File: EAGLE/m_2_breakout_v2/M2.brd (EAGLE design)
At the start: 73.3 x 101.6 mm, 55 parts, among them X1 C-GRID-14-70543, X2 C-GRID-14-70543

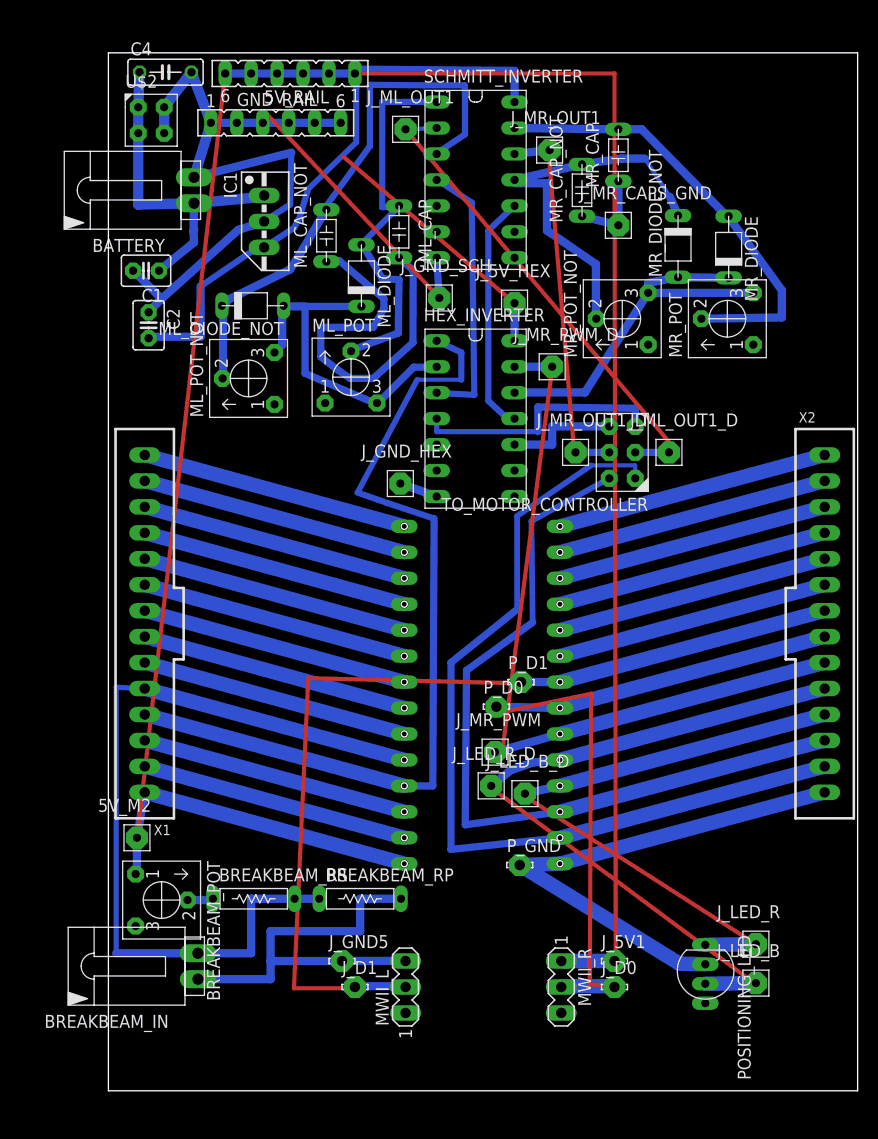
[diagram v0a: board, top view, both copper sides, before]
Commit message: Added switch for rink side
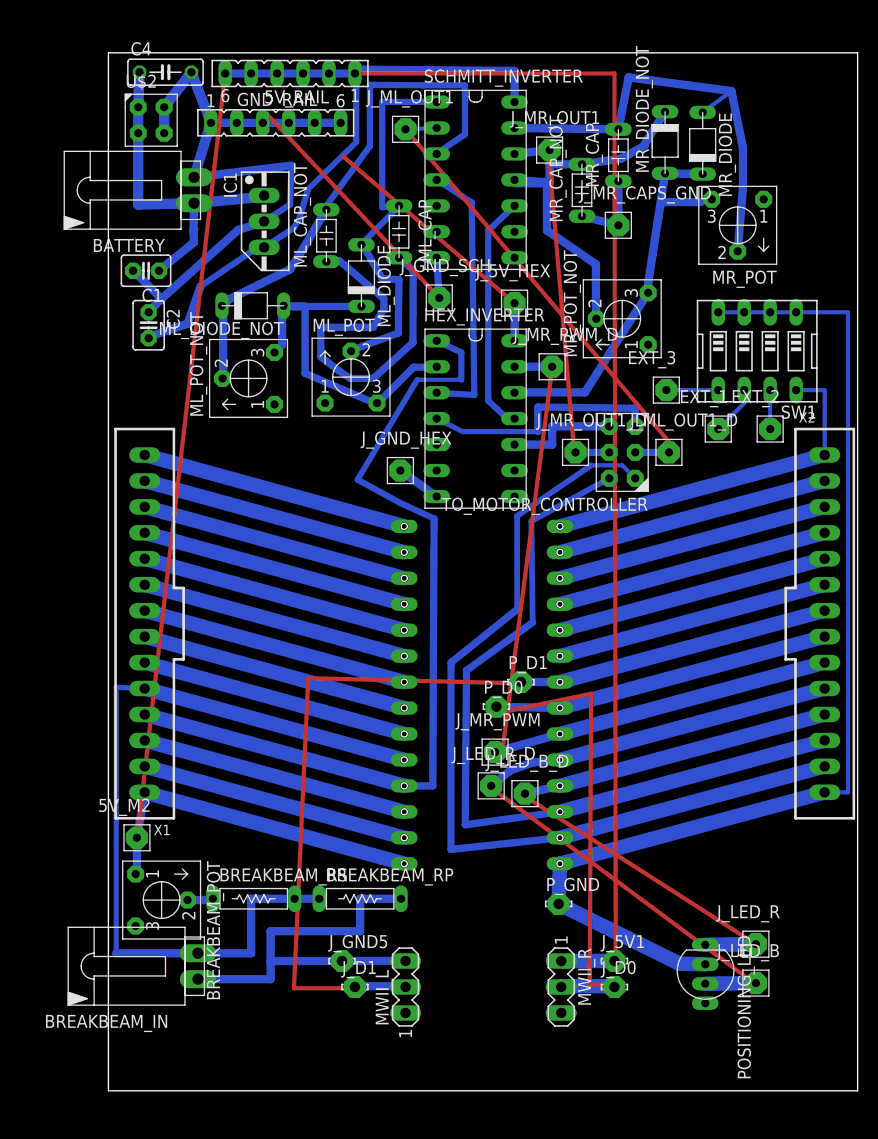
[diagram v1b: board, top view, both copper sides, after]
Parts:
- added EXT_1, EXT_2, EXT_3: ARDUINO_HEADER_1X1_OCTAGON, ben_kramer:ARDUINO_HEADER_1X1_OCTAGON
- added SW1: (no value), special:EDG-04
- moved MR_POT 11.8 mm to (61.6, 87.2), turned to 180 degrees
- moved MR_DIODE 10.5 mm to (58.2, 92.6)
- moved MR_DIODE_NOT 10.2 mm to (54.5, 93.0)
- moved P_GND 5.39 mm to (44.1, 18.3)
- moved J_GND_HEX 1.27 mm to (28.6, 60.7)
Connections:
- removed net N$17: POSITIONING_LED.GND, P_GND.MP, U$1.GND, X2.14
- new net N$14: EXT_1.1, SW1.6
- new net N$16: EXT_3.1, SW1.5
- new net N$3: POSITIONING_LED.GND, P_GND.MP, SW1.1, SW1.2, SW1.3, SW1.4, U$1.GND, X2.14
- new net N$5: EXT_2.1, SW1.7
- net N$29: now also SW1.8
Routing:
- net N$3: track 0.00 -> 108.5 mm
- net N$17: track 51.7 -> 0.00 mm
- net MR_PWM_NOT: track 37.6 -> 47.8 mm
- net N$29: track 26.8 -> 36.0 mm
- net N$16: track 0.00 -> 5.08 mm
- net N$14: track 0.00 -> 4.86 mm
- net N$5: track 0.00 -> 3.81 mm
- net 5V: track 149.4 -> 147.3 mm
- net IN_GND: track 66.9 -> 65.4 mm
- net ML_OUT2: track 24.9 -> 23.9 mm
- net ML_EN: track 87.7 -> 86.9 mm
- net ML_PWM: track 85.4 -> 84.8 mm
- net GND_HEX: track 3.78 -> 4.37 mm
- net N$4: track 38.7 -> 38.1 mm
